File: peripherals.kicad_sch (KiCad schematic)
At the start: 10 parts, among them J10 perslot3ad, J11 perslot4ad, J12 perslot3c, J13 perslot4c, J14 peridcad, J15 peridcc, J6 perslot1ad, J7 perslot1c, J8 perslot2ad, J9 perslot2c

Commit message: done the pcb layout + added the 1M ram bank project
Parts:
- J12, J13, J7, J9: footprint (none) -> Connector_PCBEdge:55308432
- J15: footprint (none) -> Connector_IDC:IDC-Header_2x15_P2.54mm_Horizontal
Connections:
- net +5V: now also J12.19 (Pin_19), J13.19 (Pin_19), J15.12 (Pin_12), J15.13 (Pin_13), J15.14 (Pin_14), J7.19 (Pin_19), J9.19 (Pin_19); no longer J12.20 (Pin_20), J13.20 (Pin_20), J15.17 (Pin_17), J15.18 (Pin_18), J15.20 (Pin_20), J7.20 (Pin_20), J9.20 (Pin_20)
- net AC.~{D}: now also J12.5 (Pin_5), J13.5 (Pin_5), J15.26 (Pin_26), J7.5 (Pin_5), J9.5 (Pin_5); no longer J12.6 (Pin_6), J13.6 (Pin_6), J15.6 (Pin_6), J7.6 (Pin_6), J9.6 (Pin_6)
- net AC.~{P}: now also J12.3 (Pin_3), J13.3 (Pin_3), J15.28 (Pin_28), J7.3 (Pin_3), J9.3 (Pin_3); no longer J12.4 (Pin_4), J13.4 (Pin_4), J15.4 (Pin_4), J7.4 (Pin_4), J9.4 (Pin_4)
- net AC.~{U}: now also J12.7 (Pin_7), J13.7 (Pin_7), J15.24 (Pin_24), J7.7 (Pin_7), J9.7 (Pin_7); no longer J12.8 (Pin_8), J13.8 (Pin_8), J15.8 (Pin_8), J7.8 (Pin_8), J9.8 (Pin_8)
- net A_{10}: now also J10.11 (Pin_11), J11.11 (Pin_11), J14.40 (Pin_40), J6.11 (Pin_11), J8.11 (Pin_11); no longer J10.12 (Pin_12), J11.12 (Pin_12), J14.12 (Pin_12), J6.12 (Pin_12), J8.12 (Pin_12)
- net A_{11}: now also J10.14 (Pin_14), J11.14 (Pin_14), J14.37 (Pin_37), J6.14 (Pin_14), J8.14 (Pin_14); no longer J10.13 (Pin_13), J11.13 (Pin_13), J14.13 (Pin_13), J6.13 (Pin_13), J8.13 (Pin_13)
- net A_{1}: now also J10.4 (Pin_4), J11.4 (Pin_4), J14.47 (Pin_47), J6.4 (Pin_4), J8.4 (Pin_4); no longer J10.3 (Pin_3), J11.3 (Pin_3), J14.3 (Pin_3), J6.3 (Pin_3), J8.3 (Pin_3)
- net A_{2}: now also J10.3 (Pin_3), J11.3 (Pin_3), J14.48 (Pin_48), J6.3 (Pin_3), J8.3 (Pin_3); no longer J10.4 (Pin_4), J11.4 (Pin_4), J14.4 (Pin_4), J6.4 (Pin_4), J8.4 (Pin_4)
- net A_{3}: now also J10.6 (Pin_6), J11.6 (Pin_6), J14.45 (Pin_45), J6.6 (Pin_6), J8.6 (Pin_6); no longer J10.5 (Pin_5), J11.5 (Pin_5), J14.5 (Pin_5), J6.5 (Pin_5), J8.5 (Pin_5)
- net A_{4}: now also J10.5 (Pin_5), J11.5 (Pin_5), J14.46 (Pin_46), J6.5 (Pin_5), J8.5 (Pin_5); no longer J10.6 (Pin_6), J11.6 (Pin_6), J14.6 (Pin_6), J6.6 (Pin_6), J8.6 (Pin_6)
- net A_{5}: now also J10.8 (Pin_8), J11.8 (Pin_8), J14.43 (Pin_43), J6.8 (Pin_8), J8.8 (Pin_8); no longer J10.7 (Pin_7), J11.7 (Pin_7), J14.7 (Pin_7), J6.7 (Pin_7), J8.7 (Pin_7)
- net A_{6}: now also J10.7 (Pin_7), J11.7 (Pin_7), J14.44 (Pin_44), J6.7 (Pin_7), J8.7 (Pin_7); no longer J10.8 (Pin_8), J11.8 (Pin_8), J14.8 (Pin_8), J6.8 (Pin_8), J8.8 (Pin_8)
- net A_{7}: now also J10.10 (Pin_10), J11.10 (Pin_10), J14.41 (Pin_41), J6.10 (Pin_10), J8.10 (Pin_10); no longer J10.9 (Pin_9), J11.9 (Pin_9), J14.9 (Pin_9), J6.9 (Pin_9), J8.9 (Pin_9)
- net A_{8}: now also J10.9 (Pin_9), J11.9 (Pin_9), J14.42 (Pin_42), J6.9 (Pin_9), J8.9 (Pin_9); no longer J10.10 (Pin_10), J11.10 (Pin_10), J14.10 (Pin_10), J6.10 (Pin_10), J8.10 (Pin_10)
- net A_{9}: now also J10.12 (Pin_12), J11.12 (Pin_12), J14.39 (Pin_39), J6.12 (Pin_12), J8.12 (Pin_12); no longer J10.11 (Pin_11), J11.11 (Pin_11), J14.11 (Pin_11), J6.11 (Pin_11), J8.11 (Pin_11)
- net CLK: now also J12.28 (Pin_28), J13.28 (Pin_28), J15.3 (Pin_3), J7.28 (Pin_28), J9.28 (Pin_28); no longer J12.27 (Pin_27), J13.27 (Pin_27), J15.27 (Pin_27), J7.27 (Pin_27), J9.27 (Pin_27)
- net DIR.~{R}: now also J10.47 (Pin_47), J11.47 (Pin_47), J14.4 (Pin_4), J6.47 (Pin_47), J8.47 (Pin_47); no longer J10.48 (Pin_48), J11.48 (Pin_48), J14.48 (Pin_48), J6.48 (Pin_48), J8.48 (Pin_48)
- net DIR.~{W}: now also J10.48 (Pin_48), J11.48 (Pin_48), J14.3 (Pin_3), J6.48 (Pin_48), J8.48 (Pin_48); no longer J10.47 (Pin_47), J11.47 (Pin_47), J14.47 (Pin_47), J6.47 (Pin_47), J8.47 (Pin_47)
- net DRD: now also J12.21 (Pin_21), J13.21 (Pin_21), J15.10 (Pin_10), J7.21 (Pin_21), J9.21 (Pin_21); no longer J12.22 (Pin_22), J13.22 (Pin_22), J15.22 (Pin_22), J7.22 (Pin_22), J9.22 (Pin_22)
- net DS.~{L}: now also J10.43 (Pin_43), J11.43 (Pin_43), J14.8 (Pin_8), J6.43 (Pin_43), J8.43 (Pin_43); no longer J10.44 (Pin_44), J11.44 (Pin_44), J14.44 (Pin_44), J6.44 (Pin_44), J8.44 (Pin_44)
- net DS.~{U}: now also J10.44 (Pin_44), J11.44 (Pin_44), J14.7 (Pin_7), J6.44 (Pin_44), J8.44 (Pin_44); no longer J10.43 (Pin_43), J11.43 (Pin_43), J14.43 (Pin_43), J6.43 (Pin_43), J8.43 (Pin_43)
- net D_{0}: now also J10.28 (Pin_28), J11.28 (Pin_28), J14.23 (Pin_23), J6.28 (Pin_28), J8.28 (Pin_28); no longer J10.27 (Pin_27), J11.27 (Pin_27), J14.27 (Pin_27), J6.27 (Pin_27), J8.27 (Pin_27)
- net D_{10}: now also J10.38 (Pin_38), J11.38 (Pin_38), J14.13 (Pin_13), J6.38 (Pin_38), J8.38 (Pin_38); no longer J10.37 (Pin_37), J11.37 (Pin_37), J14.37 (Pin_37), J6.37 (Pin_37), J8.37 (Pin_37)
- net D_{11}: now also J10.37 (Pin_37), J11.37 (Pin_37), J14.14 (Pin_14), J6.37 (Pin_37), J8.37 (Pin_37); no longer J10.38 (Pin_38), J11.38 (Pin_38), J14.38 (Pin_38), J6.38 (Pin_38), J8.38 (Pin_38)
- net D_{12}: now also J10.40 (Pin_40), J11.40 (Pin_40), J14.11 (Pin_11), J6.40 (Pin_40), J8.40 (Pin_40); no longer J10.39 (Pin_39), J11.39 (Pin_39), J14.39 (Pin_39), J6.39 (Pin_39), J8.39 (Pin_39)
- net D_{13}: now also J10.39 (Pin_39), J11.39 (Pin_39), J14.12 (Pin_12), J6.39 (Pin_39), J8.39 (Pin_39); no longer J10.40 (Pin_40), J11.40 (Pin_40), J14.40 (Pin_40), J6.40 (Pin_40), J8.40 (Pin_40)
- net D_{14}: now also J10.42 (Pin_42), J11.42 (Pin_42), J14.9 (Pin_9), J6.42 (Pin_42), J8.42 (Pin_42); no longer J10.41 (Pin_41), J11.41 (Pin_41), J14.41 (Pin_41), J6.41 (Pin_41), J8.41 (Pin_41)
- net D_{15}: now also J10.41 (Pin_41), J11.41 (Pin_41), J14.10 (Pin_10), J6.41 (Pin_41), J8.41 (Pin_41); no longer J10.42 (Pin_42), J11.42 (Pin_42), J14.42 (Pin_42), J6.42 (Pin_42), J8.42 (Pin_42)
- net D_{1}: now also J10.27 (Pin_27), J11.27 (Pin_27), J14.24 (Pin_24), J6.27 (Pin_27), J8.27 (Pin_27); no longer J10.28 (Pin_28), J11.28 (Pin_28), J14.28 (Pin_28), J6.28 (Pin_28), J8.28 (Pin_28)
- net D_{2}: now also J10.30 (Pin_30), J11.30 (Pin_30), J14.21 (Pin_21), J6.30 (Pin_30), J8.30 (Pin_30); no longer J10.29 (Pin_29), J11.29 (Pin_29), J14.29 (Pin_29), J6.29 (Pin_29), J8.29 (Pin_29)
- net D_{3}: now also J10.29 (Pin_29), J11.29 (Pin_29), J14.22 (Pin_22), J6.29 (Pin_29), J8.29 (Pin_29); no longer J10.30 (Pin_30), J11.30 (Pin_30), J14.30 (Pin_30), J6.30 (Pin_30), J8.30 (Pin_30)
- net D_{4}: now also J10.32 (Pin_32), J11.32 (Pin_32), J14.19 (Pin_19), J6.32 (Pin_32), J8.32 (Pin_32); no longer J10.31 (Pin_31), J11.31 (Pin_31), J14.31 (Pin_31), J6.31 (Pin_31), J8.31 (Pin_31)
- net D_{5}: now also J10.31 (Pin_31), J11.31 (Pin_31), J14.20 (Pin_20), J6.31 (Pin_31), J8.31 (Pin_31); no longer J10.32 (Pin_32), J11.32 (Pin_32), J14.32 (Pin_32), J6.32 (Pin_32), J8.32 (Pin_32)
- net D_{6}: now also J10.34 (Pin_34), J11.34 (Pin_34), J14.17 (Pin_17), J6.34 (Pin_34), J8.34 (Pin_34); no longer J10.33 (Pin_33), J11.33 (Pin_33), J14.33 (Pin_33), J6.33 (Pin_33), J8.33 (Pin_33)
- net D_{7}: now also J10.33 (Pin_33), J11.33 (Pin_33), J14.18 (Pin_18), J6.33 (Pin_33), J8.33 (Pin_33); no longer J10.34 (Pin_34), J11.34 (Pin_34), J14.34 (Pin_34), J6.34 (Pin_34), J8.34 (Pin_34)
- net D_{8}: now also J10.36 (Pin_36), J11.36 (Pin_36), J14.15 (Pin_15), J6.36 (Pin_36), J8.36 (Pin_36); no longer J10.35 (Pin_35), J11.35 (Pin_35), J14.35 (Pin_35), J6.35 (Pin_35), J8.35 (Pin_35)
- net D_{9}: now also J10.35 (Pin_35), J11.35 (Pin_35), J14.16 (Pin_16), J6.35 (Pin_35), J8.35 (Pin_35); no longer J10.36 (Pin_36), J11.36 (Pin_36), J14.36 (Pin_36), J6.36 (Pin_36), J8.36 (Pin_36)
- net E_{0}: now also J10.21 (Pin_21), J11.21 (Pin_21), J14.30 (Pin_30), J6.21 (Pin_21), J8.21 (Pin_21); no longer J10.22 (Pin_22), J11.22 (Pin_22), J14.22 (Pin_22), J6.22 (Pin_22), J8.22 (Pin_22)
- net E_{10}: now also J10.15 (Pin_15), J11.15 (Pin_15), J14.36 (Pin_36), J6.15 (Pin_15), J8.15 (Pin_15); no longer J10.16 (Pin_16), J11.16 (Pin_16), J14.16 (Pin_16), J6.16 (Pin_16), J8.16 (Pin_16)
- net E_{11}: now also J10.18 (Pin_18), J11.18 (Pin_18), J14.33 (Pin_33), J6.18 (Pin_18), J8.18 (Pin_18); no longer J10.17 (Pin_17), J11.17 (Pin_17), J14.17 (Pin_17), J6.17 (Pin_17), J8.17 (Pin_17)
- net E_{12}: now also J10.17 (Pin_17), J11.17 (Pin_17), J14.34 (Pin_34), J6.17 (Pin_17), J8.17 (Pin_17); no longer J10.18 (Pin_18), J11.18 (Pin_18), J14.18 (Pin_18), J6.18 (Pin_18), J8.18 (Pin_18)
- net E_{13}: now also J10.20 (Pin_20), J11.20 (Pin_20), J14.31 (Pin_31), J6.20 (Pin_20), J8.20 (Pin_20); no longer J10.19 (Pin_19), J11.19 (Pin_19), J14.19 (Pin_19), J6.19 (Pin_19), J8.19 (Pin_19)
- net E_{14}: now also J10.19 (Pin_19), J11.19 (Pin_19), J14.32 (Pin_32), J6.19 (Pin_19), J8.19 (Pin_19); no longer J10.20 (Pin_20), J11.20 (Pin_20), J14.20 (Pin_20), J6.20 (Pin_20), J8.20 (Pin_20)
- net E_{15}: now also J10.22 (Pin_22), J11.22 (Pin_22), J14.29 (Pin_29), J6.22 (Pin_22), J8.22 (Pin_22); no longer J10.21 (Pin_21), J11.21 (Pin_21), J14.21 (Pin_21), J6.21 (Pin_21), J8.21 (Pin_21)
- net E_{1}: now also J10.24 (Pin_24), J11.24 (Pin_24), J14.27 (Pin_27), J6.24 (Pin_24), J8.24 (Pin_24); no longer J10.23 (Pin_23), J11.23 (Pin_23), J14.23 (Pin_23), J6.23 (Pin_23), J8.23 (Pin_23)
- net E_{2}: now also J10.23 (Pin_23), J11.23 (Pin_23), J14.28 (Pin_28), J6.23 (Pin_23), J8.23 (Pin_23); no longer J10.24 (Pin_24), J11.24 (Pin_24), J14.24 (Pin_24), J6.24 (Pin_24), J8.24 (Pin_24)
- net E_{3}: now also J10.26 (Pin_26), J11.26 (Pin_26), J6.26 (Pin_26), J8.26 (Pin_26); no longer J10.25 (Pin_25), J11.25 (Pin_25), J6.25 (Pin_25), J8.25 (Pin_25)
- net E_{5}: now also J12.4 (Pin_4), J13.4 (Pin_4), J15.27 (Pin_27), J7.4 (Pin_4), J9.4 (Pin_4); no longer J12.3 (Pin_3), J13.3 (Pin_3), J15.3 (Pin_3), J7.3 (Pin_3), J9.3 (Pin_3)
- net E_{6}: now also J12.6 (Pin_6), J13.6 (Pin_6), J15.25 (Pin_25), J7.6 (Pin_6), J9.6 (Pin_6); no longer J12.5 (Pin_5), J13.5 (Pin_5), J15.5 (Pin_5), J7.5 (Pin_5), J9.5 (Pin_5)
- net E_{7}: now also J12.8 (Pin_8), J13.8 (Pin_8), J15.23 (Pin_23), J7.8 (Pin_8), J9.8 (Pin_8); no longer J12.7 (Pin_7), J13.7 (Pin_7), J15.7 (Pin_7), J7.7 (Pin_7), J9.7 (Pin_7)
- net E_{8}: now also J10.13 (Pin_13), J11.13 (Pin_13), J14.38 (Pin_38), J6.13 (Pin_13), J8.13 (Pin_13); no longer J10.14 (Pin_14), J11.14 (Pin_14), J14.14 (Pin_14), J6.14 (Pin_14), J8.14 (Pin_14)
- net E_{9}: now also J10.16 (Pin_16), J11.16 (Pin_16), J14.35 (Pin_35), J6.16 (Pin_16), J8.16 (Pin_16); no longer J10.15 (Pin_15), J11.15 (Pin_15), J14.15 (Pin_15), J6.15 (Pin_15), J8.15 (Pin_15)
- net GND: now also J10.25 (Pin_25), J11.25 (Pin_25), J12.27 (Pin_27), J13.27 (Pin_27), J15.4 (Pin_4), J15.5 (Pin_5), J15.6 (Pin_6), J6.25 (Pin_25), J7.27 (Pin_27), J8.25 (Pin_25), J9.27 (Pin_27); no longer J10.26 (Pin_26), J11.26 (Pin_26), J12.28 (Pin_28), J13.28 (Pin_28), J15.25 (Pin_25), J15.26 (Pin_26), J15.28 (Pin_28), J6.26 (Pin_26), J7.28 (Pin_28), J8.26 (Pin_26), J9.28 (Pin_28)
- net IBSY: now also J12.20 (Pin_20), J13.20 (Pin_20), J15.11 (Pin_11), J7.20 (Pin_20), J9.20 (Pin_20); no longer J12.19 (Pin_19), J13.19 (Pin_19), J15.19 (Pin_19), J7.19 (Pin_19), J9.19 (Pin_19)
- net IRQ_{0}: now also J12.10 (Pin_10), J13.10 (Pin_10), J15.21 (Pin_21), J7.10 (Pin_10), J9.10 (Pin_10); no longer J12.9 (Pin_9), J13.9 (Pin_9), J15.9 (Pin_9), J7.9 (Pin_9), J9.9 (Pin_9)
- net IRQ_{1}: now also J12.9 (Pin_9), J13.9 (Pin_9), J15.22 (Pin_22), J7.9 (Pin_9), J9.9 (Pin_9); no longer J12.10 (Pin_10), J13.10 (Pin_10), J15.10 (Pin_10), J7.10 (Pin_10), J9.10 (Pin_10)
- net IRQ_{2}: now also J12.12 (Pin_12), J13.12 (Pin_12), J15.19 (Pin_19), J7.12 (Pin_12), J9.12 (Pin_12); no longer J12.11 (Pin_11), J13.11 (Pin_11), J15.11 (Pin_11), J7.11 (Pin_11), J9.11 (Pin_11)
- net IRQ_{3}: now also J12.11 (Pin_11), J13.11 (Pin_11), J15.20 (Pin_20), J7.11 (Pin_11), J9.11 (Pin_11); no longer J12.12 (Pin_12), J13.12 (Pin_12), J15.12 (Pin_12), J7.12 (Pin_12), J9.12 (Pin_12)
- net IRQ_{4}: now also J12.14 (Pin_14), J13.14 (Pin_14), J15.17 (Pin_17), J7.14 (Pin_14), J9.14 (Pin_14); no longer J12.13 (Pin_13), J13.13 (Pin_13), J15.13 (Pin_13), J7.13 (Pin_13), J9.13 (Pin_13)
- net IRQ_{5}: now also J12.13 (Pin_13), J13.13 (Pin_13), J15.18 (Pin_18), J7.13 (Pin_13), J9.13 (Pin_13); no longer J12.14 (Pin_14), J13.14 (Pin_14), J15.14 (Pin_14), J7.14 (Pin_14), J9.14 (Pin_14)
- net IRQ_{6}: now also J12.16 (Pin_16), J13.16 (Pin_16), J7.16 (Pin_16), J9.16 (Pin_16); no longer J12.15 (Pin_15), J13.15 (Pin_15), J7.15 (Pin_15), J9.15 (Pin_15)
- net IRQ_{7}: now also J12.15 (Pin_15), J13.15 (Pin_15), J7.15 (Pin_15), J9.15 (Pin_15); no longer J12.16 (Pin_16), J13.16 (Pin_16), J7.16 (Pin_16), J9.16 (Pin_16)
- net ~{HALT}: now also J12.23 (Pin_23), J13.23 (Pin_23), J15.8 (Pin_8), J7.23 (Pin_23), J9.23 (Pin_23); no longer J12.24 (Pin_24), J13.24 (Pin_24), J15.24 (Pin_24), J7.24 (Pin_24), J9.24 (Pin_24)
- net ~{RES}: now also J12.24 (Pin_24), J13.24 (Pin_24), J15.7 (Pin_7), J7.24 (Pin_24), J9.24 (Pin_24); no longer J12.23 (Pin_23), J13.23 (Pin_23), J15.23 (Pin_23), J7.23 (Pin_23), J9.23 (Pin_23)
- net ~{RIH}: now also J12.22 (Pin_22), J13.22 (Pin_22), J15.9 (Pin_9), J7.22 (Pin_22), J9.22 (Pin_22); no longer J12.21 (Pin_21), J13.21 (Pin_21), J15.21 (Pin_21), J7.21 (Pin_21), J9.21 (Pin_21)
- net ~{IO} renamed BE.~{M}
- net BE.~{M}: now also J14.6 (Pin_6); no longer J14.45 (Pin_45)
- net ~{M} renamed BE.~{IO}
- net BE.~{IO}: now also J14.5 (Pin_5); no longer J14.46 (Pin_46)
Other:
- moved on the sheet: J14, J15

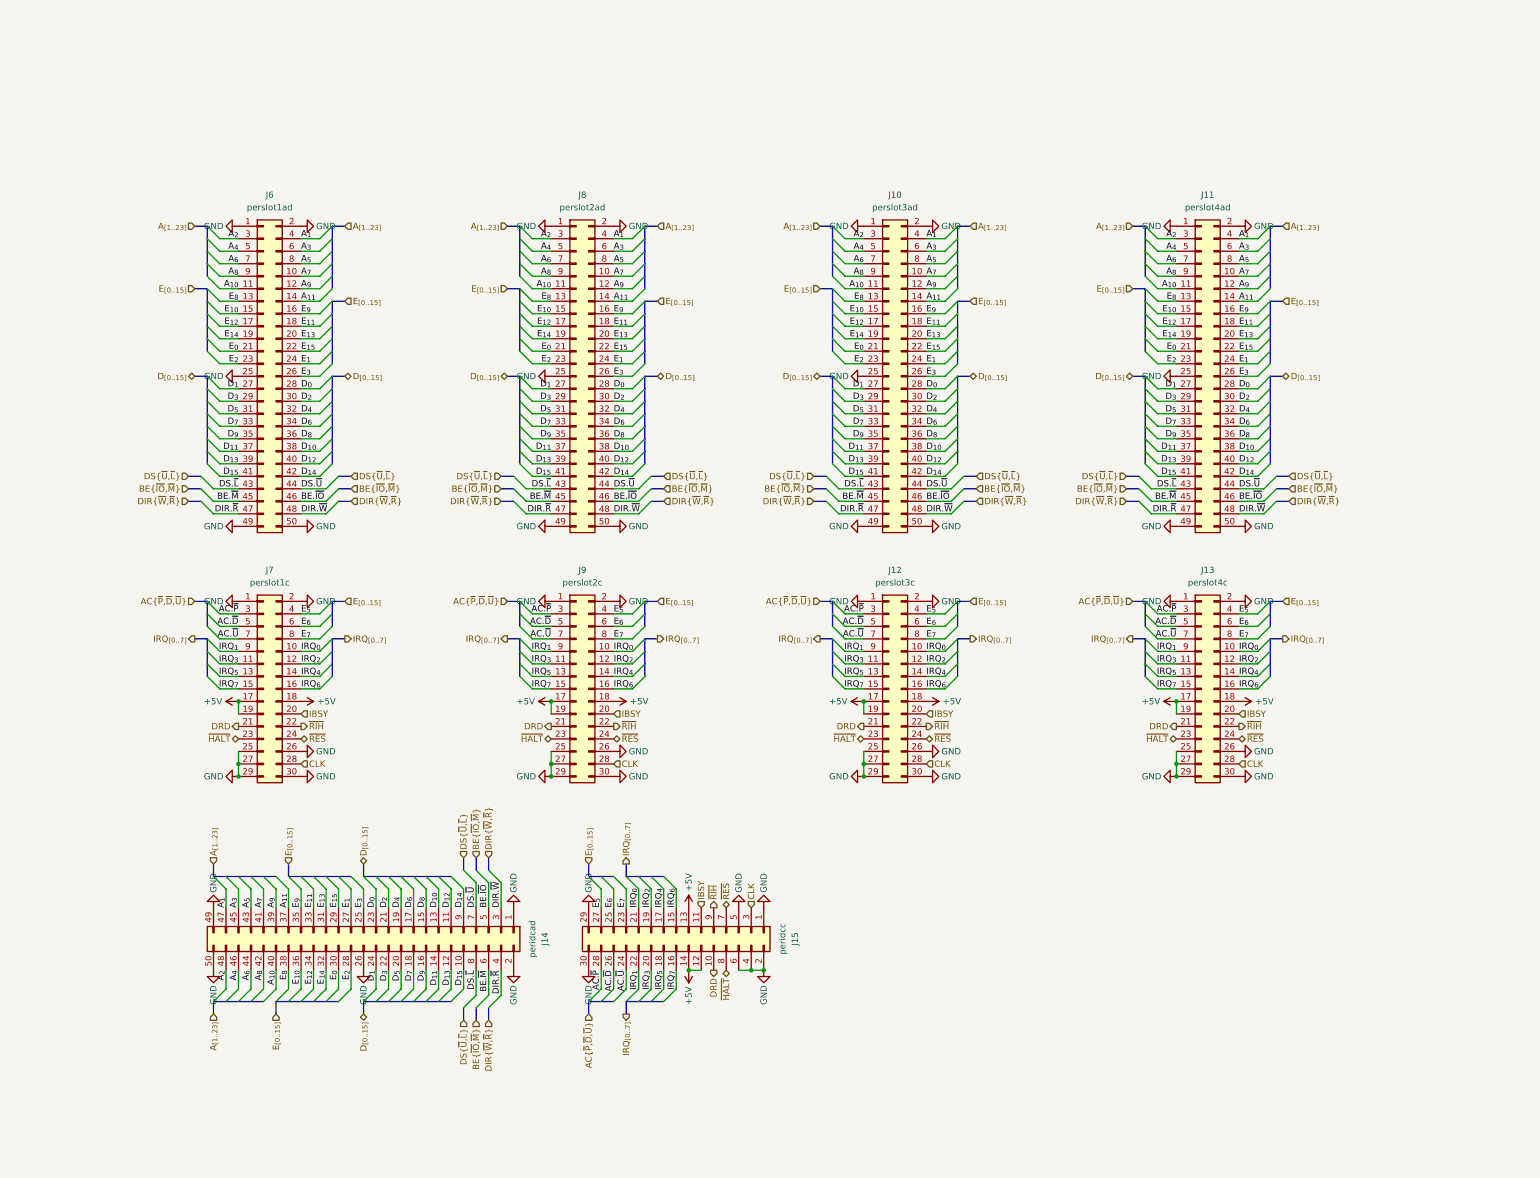
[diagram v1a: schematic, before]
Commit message: updated scheme: 	- fixed E to P & PRT mapping 	- swapped root's 04 couple with the 14's of pidreg & statusreg
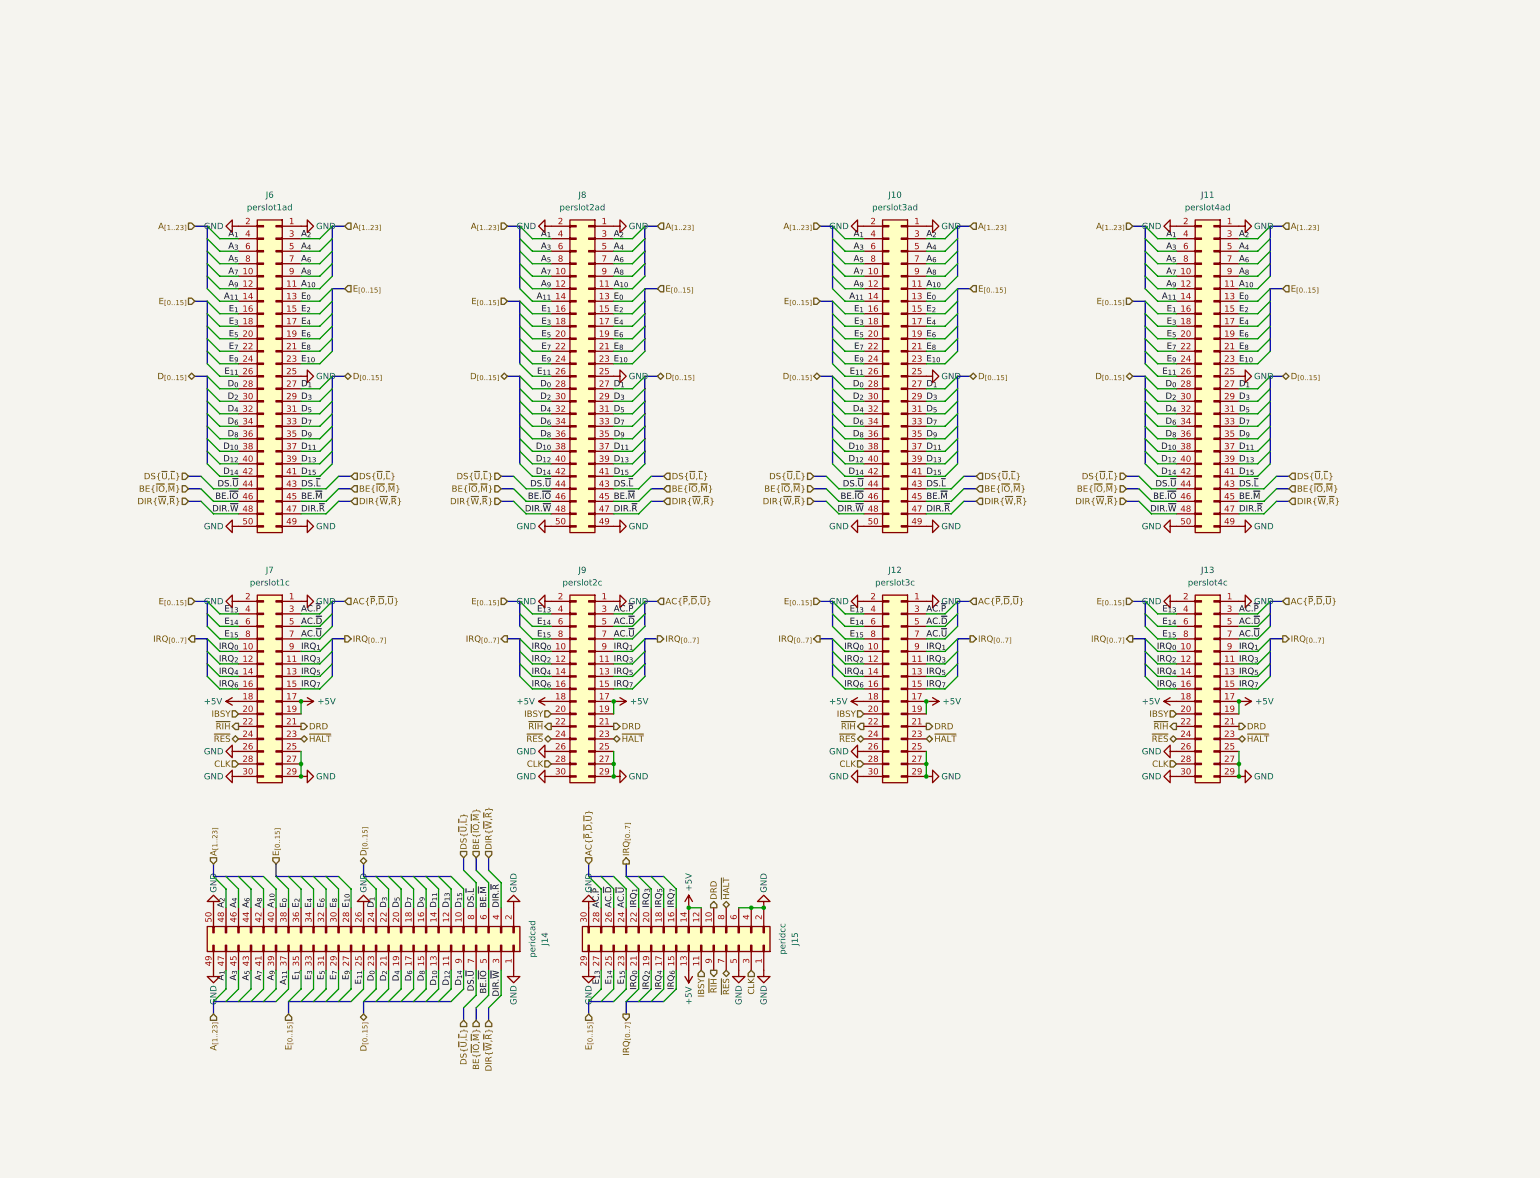
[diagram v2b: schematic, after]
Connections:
- net E_{0}: now also J10.13 (Pin_13), J11.13 (Pin_13), J14.38 (Pin_38), J6.13 (Pin_13), J8.13 (Pin_13); no longer J10.21 (Pin_21), J11.21 (Pin_21), J14.30 (Pin_30), J6.21 (Pin_21), J8.21 (Pin_21)
- net E_{10}: now also J10.23 (Pin_23), J11.23 (Pin_23), J14.28 (Pin_28), J6.23 (Pin_23), J8.23 (Pin_23); no longer J10.15 (Pin_15), J11.15 (Pin_15), J14.36 (Pin_36), J6.15 (Pin_15), J8.15 (Pin_15)
- net E_{11}: now also J10.26 (Pin_26), J11.26 (Pin_26), J14.25 (Pin_25), J6.26 (Pin_26), J8.26 (Pin_26); no longer J10.18 (Pin_18), J11.18 (Pin_18), J14.33 (Pin_33), J6.18 (Pin_18), J8.18 (Pin_18)
- net E_{13}: now also J12.4 (Pin_4), J13.4 (Pin_4), J15.27 (Pin_27), J7.4 (Pin_4), J9.4 (Pin_4); no longer J10.20 (Pin_20), J11.20 (Pin_20), J14.31 (Pin_31), J6.20 (Pin_20), J8.20 (Pin_20)
- net E_{14}: now also J12.6 (Pin_6), J13.6 (Pin_6), J15.25 (Pin_25), J7.6 (Pin_6), J9.6 (Pin_6); no longer J10.19 (Pin_19), J11.19 (Pin_19), J14.32 (Pin_32), J6.19 (Pin_19), J8.19 (Pin_19)
- net E_{15}: now also J12.8 (Pin_8), J13.8 (Pin_8), J15.23 (Pin_23), J7.8 (Pin_8), J9.8 (Pin_8); no longer J10.22 (Pin_22), J11.22 (Pin_22), J14.29 (Pin_29), J6.22 (Pin_22), J8.22 (Pin_22)
- net E_{1}: now also J10.16 (Pin_16), J11.16 (Pin_16), J14.35 (Pin_35), J6.16 (Pin_16), J8.16 (Pin_16); no longer J10.24 (Pin_24), J11.24 (Pin_24), J14.27 (Pin_27), J6.24 (Pin_24), J8.24 (Pin_24)
- net E_{2}: now also J10.15 (Pin_15), J11.15 (Pin_15), J14.36 (Pin_36), J6.15 (Pin_15), J8.15 (Pin_15); no longer J10.23 (Pin_23), J11.23 (Pin_23), J14.28 (Pin_28), J6.23 (Pin_23), J8.23 (Pin_23)
- net E_{3}: now also J10.18 (Pin_18), J11.18 (Pin_18), J14.33 (Pin_33), J6.18 (Pin_18), J8.18 (Pin_18); no longer J10.26 (Pin_26), J11.26 (Pin_26), J14.25 (Pin_25), J6.26 (Pin_26), J8.26 (Pin_26)
- net E_{5}: now also J10.20 (Pin_20), J11.20 (Pin_20), J14.31 (Pin_31), J6.20 (Pin_20), J8.20 (Pin_20); no longer J12.4 (Pin_4), J13.4 (Pin_4), J15.27 (Pin_27), J7.4 (Pin_4), J9.4 (Pin_4)
- net E_{6}: now also J10.19 (Pin_19), J11.19 (Pin_19), J14.32 (Pin_32), J6.19 (Pin_19), J8.19 (Pin_19); no longer J12.6 (Pin_6), J13.6 (Pin_6), J15.25 (Pin_25), J7.6 (Pin_6), J9.6 (Pin_6)
- net E_{7}: now also J10.22 (Pin_22), J11.22 (Pin_22), J14.29 (Pin_29), J6.22 (Pin_22), J8.22 (Pin_22); no longer J12.8 (Pin_8), J13.8 (Pin_8), J15.23 (Pin_23), J7.8 (Pin_8), J9.8 (Pin_8)
- net E_{8}: now also J10.21 (Pin_21), J11.21 (Pin_21), J14.30 (Pin_30), J6.21 (Pin_21), J8.21 (Pin_21); no longer J10.13 (Pin_13), J11.13 (Pin_13), J14.38 (Pin_38), J6.13 (Pin_13), J8.13 (Pin_13)
- net E_{9}: now also J10.24 (Pin_24), J11.24 (Pin_24), J14.27 (Pin_27), J6.24 (Pin_24), J8.24 (Pin_24); no longer J10.16 (Pin_16), J11.16 (Pin_16), J14.35 (Pin_35), J6.16 (Pin_16), J8.16 (Pin_16)
- net E_{12} renamed E_{4}
